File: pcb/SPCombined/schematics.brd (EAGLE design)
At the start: 149.8 x 71.4 mm, 102 parts

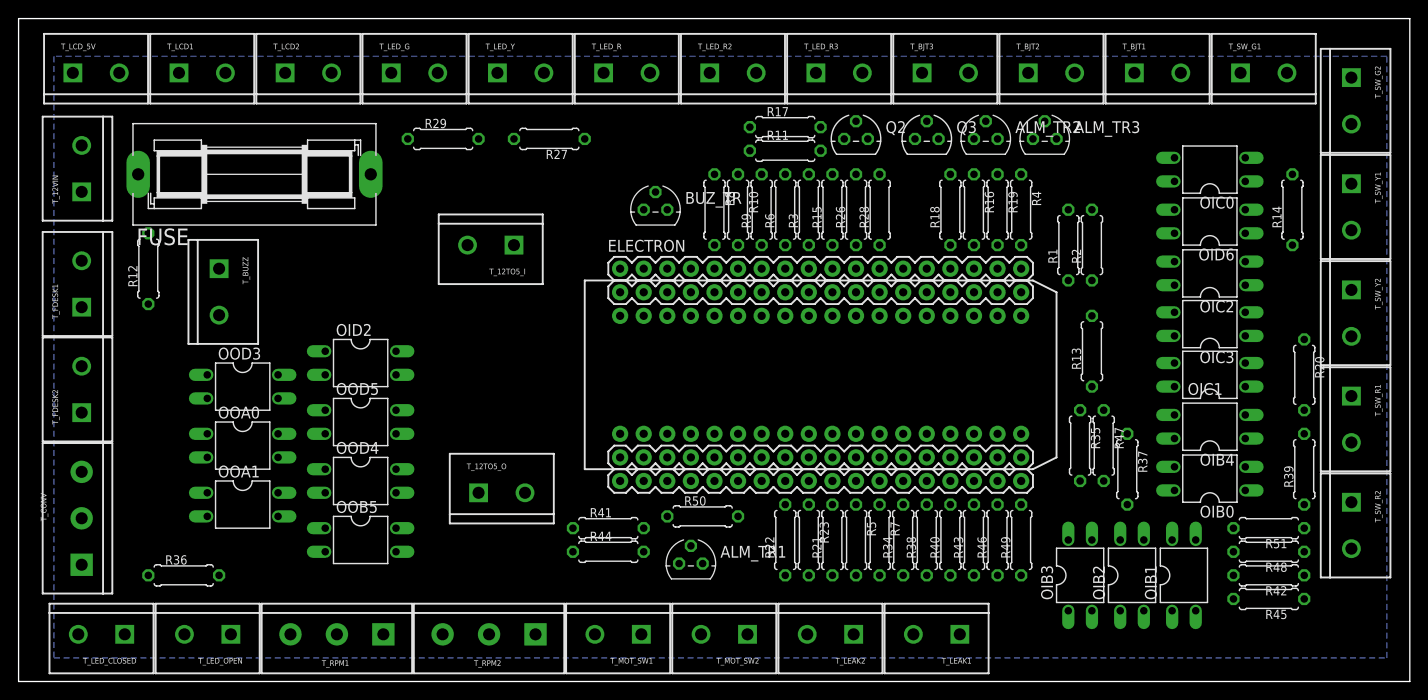
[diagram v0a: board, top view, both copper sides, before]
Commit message: PCB size 2mm margin.
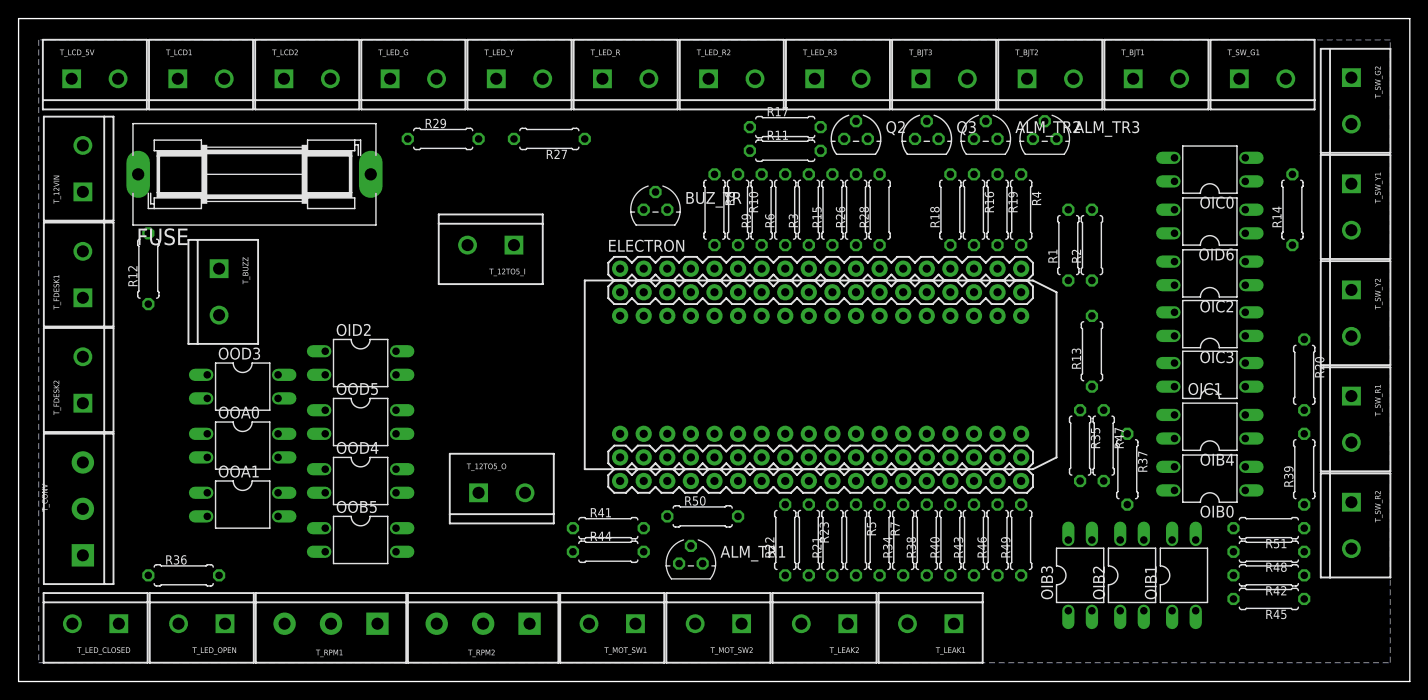
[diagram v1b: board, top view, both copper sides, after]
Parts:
- moved T_LEAK1 1.31 mm to (100.7, 6.22)
- moved T_MOT_SW2 1.31 mm to (77.9, 6.22)
- moved T_RPM1 1.31 mm to (38.6, 6.22)
- moved T_LED_CLOSED 1.31 mm to (10.8, 6.22)
- moved T_LED_OPEN 1.31 mm to (22.2, 6.22)
- moved T_RPM2 1.31 mm to (55.0, 6.22)
- moved T_LEAK2 1.31 mm to (89.3, 6.22)
- moved T_MOT_SW1 1.31 mm to (66.4, 6.22)
- moved T_FDESK1 1.02 mm to (6.92, 41.3)
- moved T_CONV 1.02 mm to (6.92, 13.6)
- moved T_FDESK2 1.02 mm to (6.92, 30.0)
- moved T_BJT2 0.65 mm to (108.6, 64.9)
- moved T_LED_R3 0.65 mm to (85.7, 64.9)
- moved T_SW_G1 0.65 mm to (131.4, 64.9)
- moved T_LCD2 0.65 mm to (28.6, 64.9)
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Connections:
- removed net GNDA: OIC3.3, OID2.3, OOA0.3, OOA1.3, OOD3.3, OOD4.3, OOD5.3, T_12TO5_I.2, T_12TO5_O.2, T_CONV.1, T_LCD2.1, T_LCD_5V.2, T_LEAK1.2, T_LEAK2.2, T_MOT_SW1.2, T_MOT_SW2.2, T_RPM2.1, T_SW_G2.1, T_SW_G2.2, T_SW_R2.1, T_SW_R2.2, T_SW_Y2.1, T_SW_Y2.2
- net GND: now also OIC3.3, OID2.3, OOA0.3, OOA1.3, OOD3.3, OOD4.3, OOD5.3, T_12TO5_I.2, T_12TO5_O.2, T_CONV.1, T_LCD2.1, T_LCD_5V.2, T_LEAK1.2, T_LEAK2.2, T_MOT_SW1.2, T_MOT_SW2.2, T_RPM2.1, T_SW_G2.1, T_SW_G2.2, T_SW_R2.1, T_SW_R2.2, T_SW_Y2.1, T_SW_Y2.2

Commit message: Save autoroute state.
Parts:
- moved R11 25.9 mm to (57.1, 52.1)
- moved R17 25.9 mm to (57.1, 54.6)
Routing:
- net +12V: track 0.00 -> 371.3 mm
- net +3V3: track 0.00 -> 205.3 mm, vias 0 -> 2
- net IN_FLO_VCC: track 0.00 -> 203.8 mm
- net N$16: track 0.00 -> 125.7 mm, vias 0 -> 1
- net N$11: track 0.00 -> 119.7 mm
- net IN_RPM2: track 0.00 -> 115.5 mm
- net SCL: track 0.00 -> 111.6 mm, vias 0 -> 1
- net N$4: track 0.00 -> 95.9 mm, vias 0 -> 1
- net SDA: track 0.00 -> 92.7 mm
- net +5V: track 0.00 -> 92.6 mm
- net N$12: track 0.00 -> 86.4 mm, vias 0 -> 1
- net N$24: track 0.00 -> 85.9 mm, vias 0 -> 1
- net INA_LVL: track 0.00 -> 82.8 mm
- net N$9: track 0.00 -> 79.6 mm, vias 0 -> 1
- net N$1: track 0.00 -> 79.3 mm, vias 0 -> 1
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
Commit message: Rereroute.
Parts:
- moved R39 123.2 mm to (15.2, 21.6)
- moved OIB4 104.3 mm to (24.1, 22.1), turned to 270 degrees
- moved OID6 92.5 mm to (36.8, 35.6), turned to 270 degrees
- moved OOD4 45.9 mm to (67.3, 55.9), turned to 90 degrees
- moved OID2 44.5 mm to (81.3, 33.0)
- moved BUZ_TR 39.9 mm to (29.2, 44.5)
- moved OOA1 27.4 mm to (50.8, 12.7)
- moved OIC0 26.7 mm to (128.3, 28.4)
- moved R14 22.9 mm to (138.4, 27.9), turned to 270 degrees
- moved OIB3 17.3 mm to (128.3, 21.6), turned to 90 degrees
- moved OIB0 17.2 mm to (114.6, 11.4), turned to 0 degrees
- moved OOA0 13.3 mm to (36.8, 21.6), turned to 90 degrees
- moved R11 12.0 mm to (68.6, 48.3)
- moved OIC2 11.4 mm to (128.3, 55.4)
- moved R36 6.48 mm to (24.1, 12.7)
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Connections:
- net N$6 renamed +12VIN
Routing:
- net +12V: track 371.3 -> 588.2 mm
- net IN_FLO_VCC: track 203.8 -> 26.4 mm
- net N$20: track 73.1 -> 183.5 mm, vias 1 -> 0
- net N$11: track 119.7 -> 26.0 mm
- net N$26: track 5.59 -> 97.7 mm, vias 0 -> 2
- net N$16: track 125.7 -> 59.3 mm
- net IN_RPM2: track 115.5 -> 53.1 mm
- net N$9: track 79.6 -> 26.8 mm
- net N$3: track 63.4 -> 12.5 mm, vias 1 -> 0
- net N$8: track 55.9 -> 11.3 mm, vias 1 -> 0
- net N$7: track 7.14 -> 50.7 mm
- net OUT_LY: track 55.6 -> 15.8 mm, vias 1 -> 0
- net OUT_LR2: track 73.9 -> 37.6 mm, vias 0 -> 1
- net N$1: track 79.3 -> 112.6 mm, vias 1 -> 0
- net N$14: track 16.9 -> 49.7 mm
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
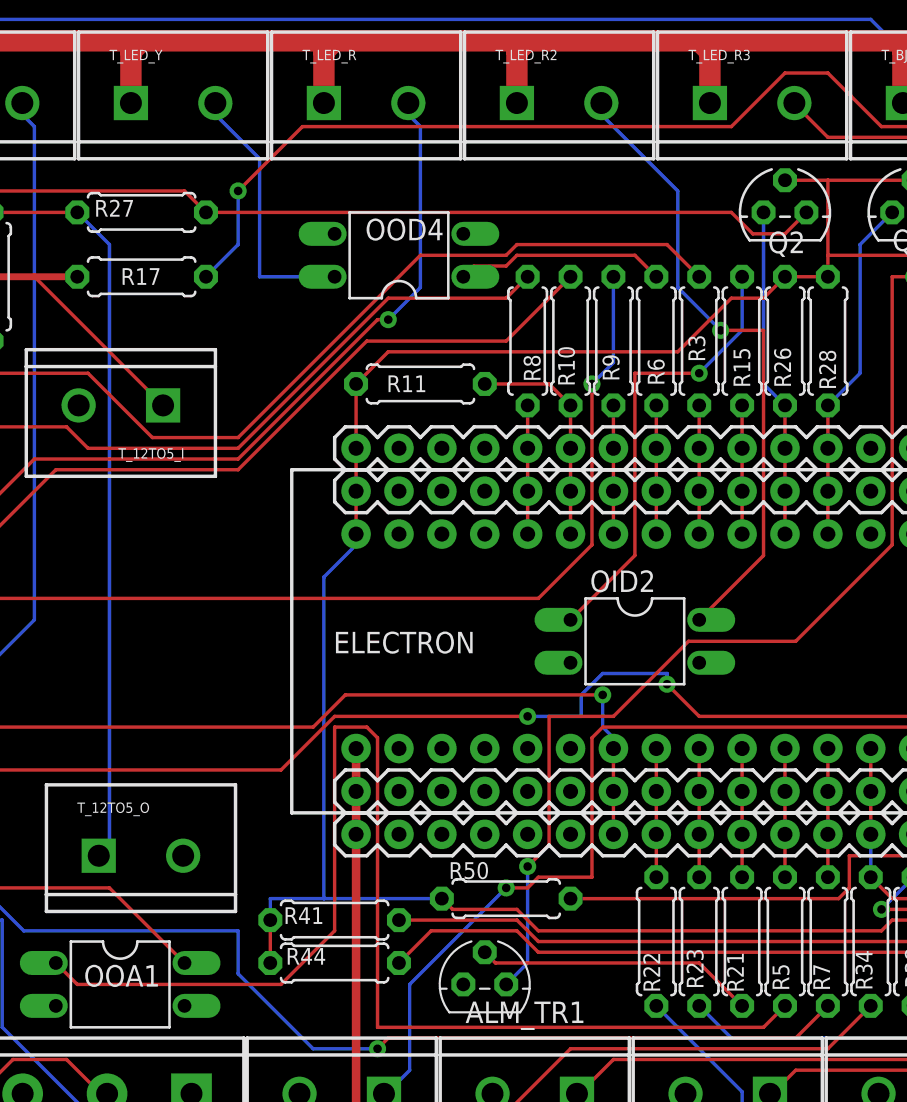
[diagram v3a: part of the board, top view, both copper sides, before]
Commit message: Add resistor values. Move out opto from electron area.
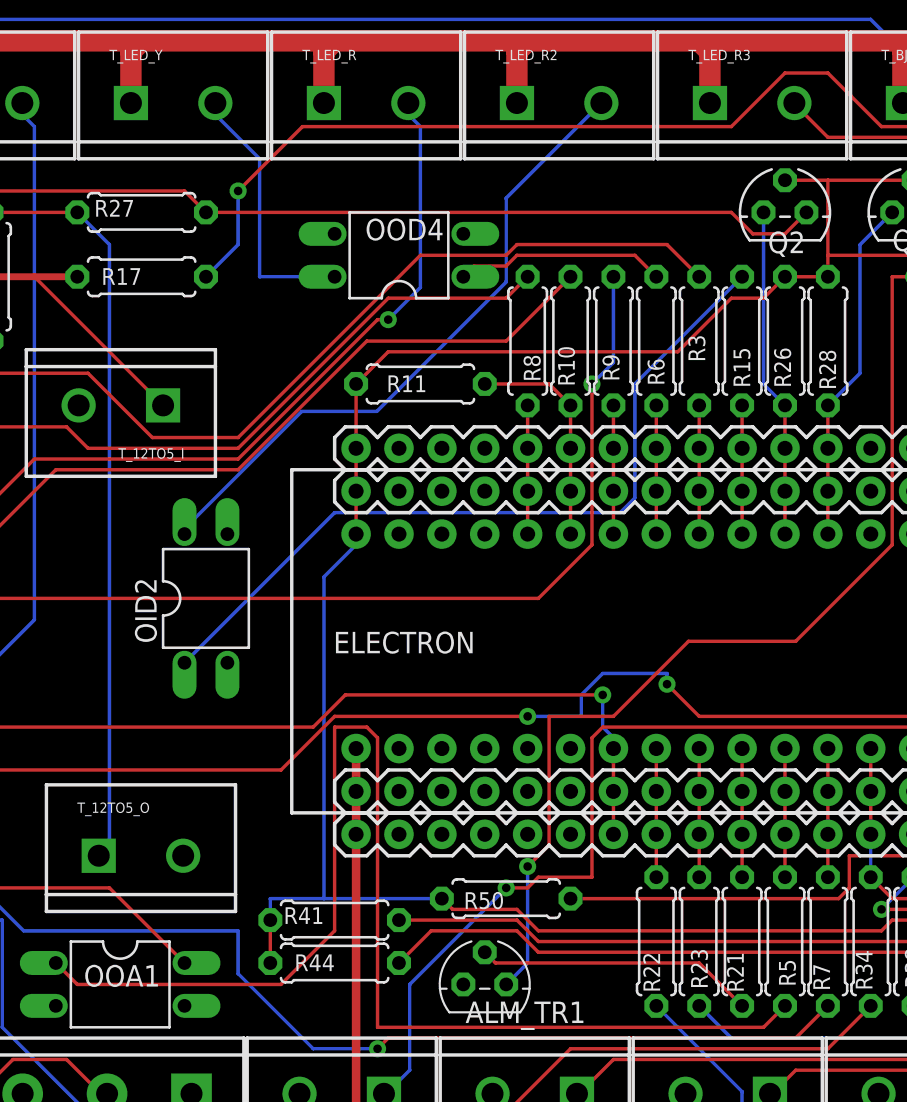
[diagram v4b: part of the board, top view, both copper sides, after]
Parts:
- R1, R10, R15, R18, R2, R3, R34, R37, R4, R40, R43, R46, R49, R5, R6, R7, R9: value (none) -> 220
- R11, R13, R16, R19, R35, R38, R41, R44, R47, R50: value (none) -> 10k
- R12, R14, R17, R20, R36, R39, R42, R45, R48, R51: value (none) -> 1k
- R21, R22, R23, R8: value (none) -> 2.2k
- moved OID2 25.5 mm to (55.9, 35.6), turned to 0 degrees
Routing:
- net N$9: track 26.8 -> 46.4 mm, vias 1 -> 0
- net OUT_LR2: track 37.6 -> 39.1 mm, vias 1 -> 0
